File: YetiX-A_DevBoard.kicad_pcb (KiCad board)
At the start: 4 copper layers, 61.3 x 20.8 mm, 58 parts, among them IC101 MCXA156VLH, J1 CONN HEADER VERT 22POS 2.54MM, J101 USB4105GFA120, J102 FTS-105-01-F-DV-P-TR, J2 CONN HEADER VERT 22POS 2.54MM, SW101 KMR421GULCLFS, SW102 KMR421GULCLFS, U1 M95256-DFMN6TP, U101 RCLAMP0854P.TCT, U102 XC6227C331PR-G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

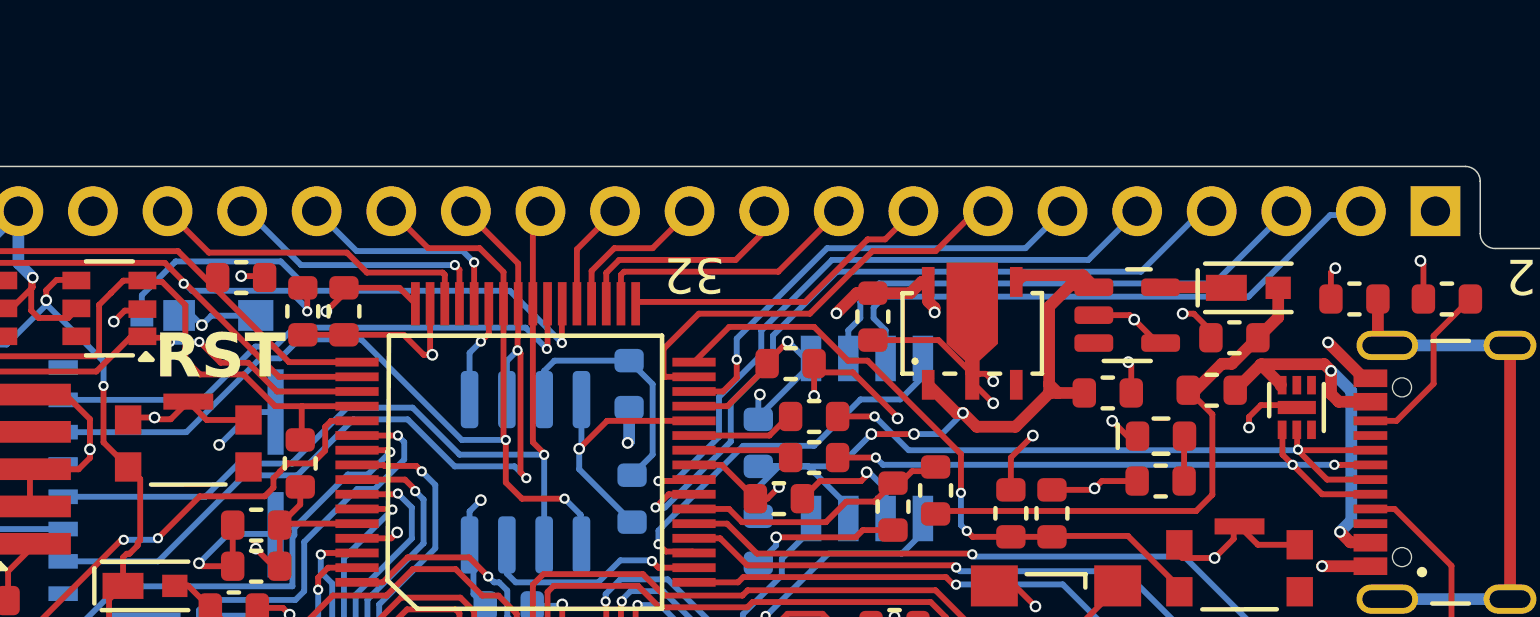
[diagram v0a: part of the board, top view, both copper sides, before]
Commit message: Rev: 0.0.2
- Added filtering capacitors on CAN output.
- Added optional CAN termination
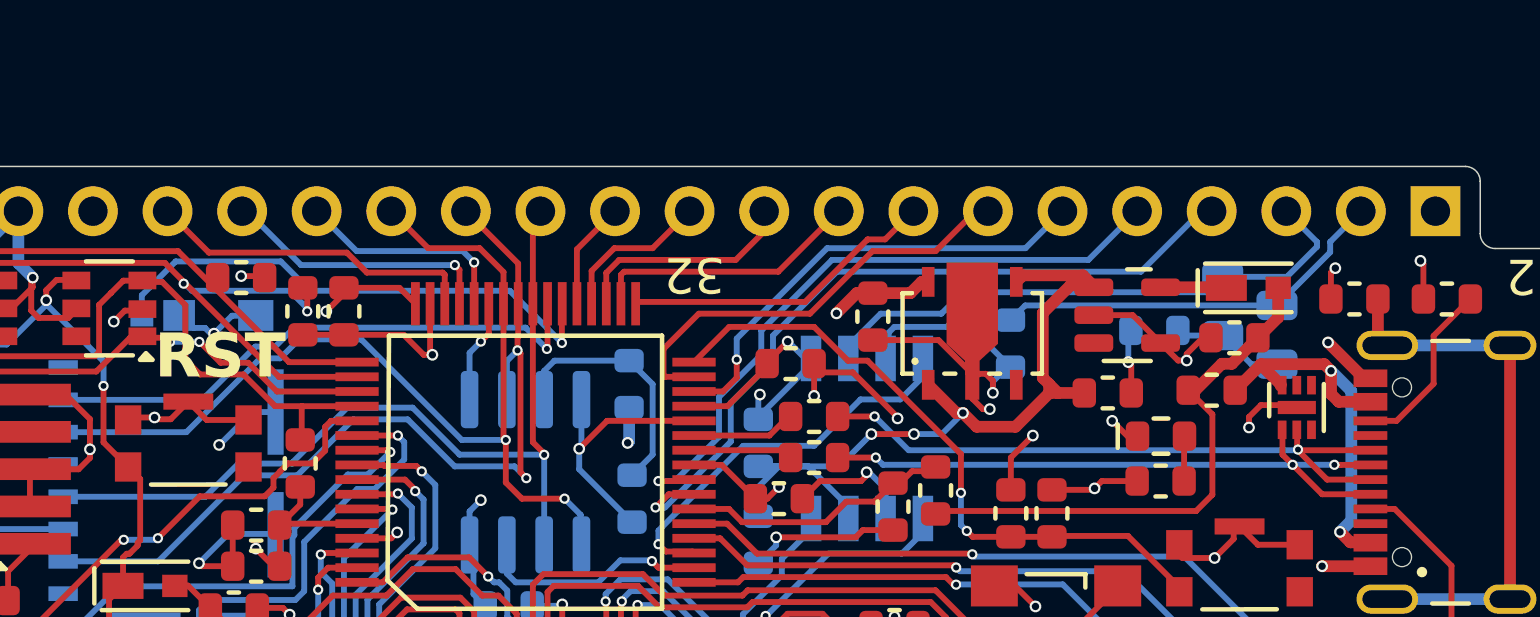
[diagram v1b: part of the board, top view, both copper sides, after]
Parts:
- added C117: 100n, passive:C_0603, B.Cu at (166.4, 95.5)
- added C3: 100p, passive:C_0603, B.Cu at (160.2, 95.0)
- added C4: 100p, passive:C_0603, B.Cu at (161.6, 96.0)
- added R3: 60R4, passive:R_0805, B.Cu at (170.6, 95.7)
- added R4: 60R4, passive:R_0805, B.Cu at (168.8, 94.7)
- moved G*** 1.60 mm to (165.5, 101.9)
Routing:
- net GND: track 107.9 -> 114.0 mm, vias 37 -> 36
- net Net-(C117-Pad2): track 0.00 -> 3.85 mm
- net /CAN-: track 18.2 -> 19.4 mm
- net +3V3: track 78.4 -> 77.2 mm, vias 17 -> 16
- net /CAN+: track 19.9 -> 18.9 mm
